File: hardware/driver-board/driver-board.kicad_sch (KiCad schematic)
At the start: 27 parts, among them J1 Conn_ARM_JTAG_SWD_10, J2 USB_C_Receptacle_USB2.0_16P, SW1 SW_Push, U1 STM32F103CBT6, U2 USBLC6-2SC6, Y1 16Mhz

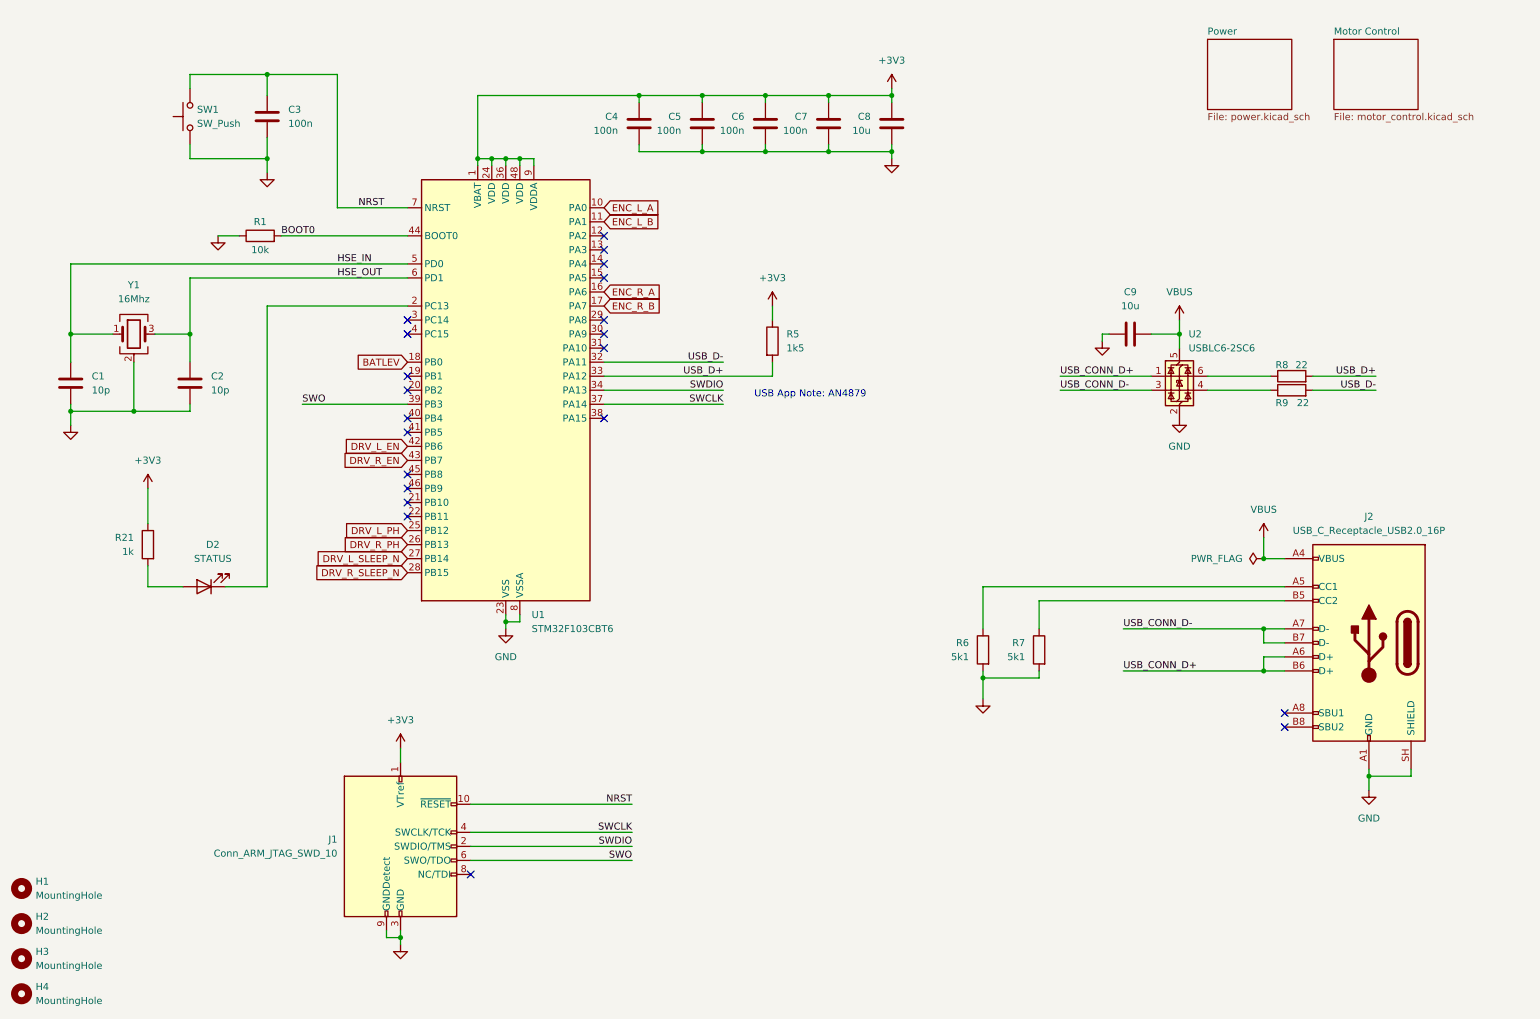
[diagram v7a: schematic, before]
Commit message: Refine Rev A PCB placement and decoupling
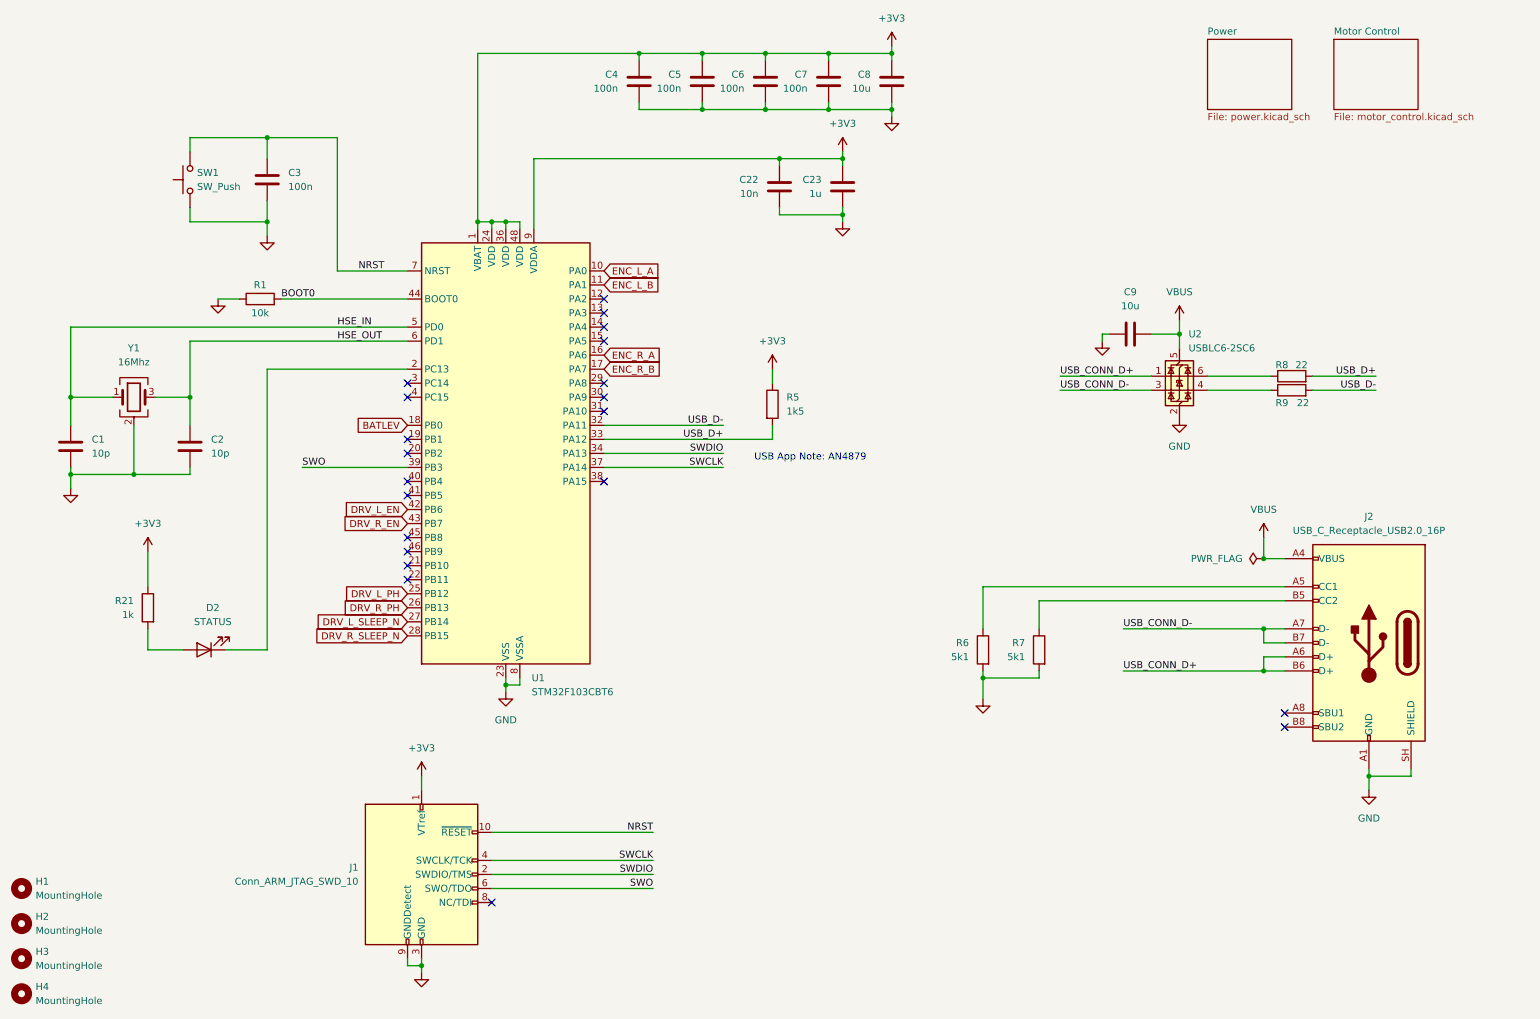
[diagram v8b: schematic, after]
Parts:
- added C22: 10n, Capacitor_SMD:C_0402_1005Metric, symbol Device:C
- added C23: 1u, Capacitor_SMD:C_0603_1608Metric, symbol Device:C
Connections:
- net +3V3: now also C22.1, C23.1
- net GND: now also C22.2, C23.2
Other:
- moved on the sheet: C1, C2, C3, C4, C5, C6, C7, C8, D2, J1, R1, R21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
